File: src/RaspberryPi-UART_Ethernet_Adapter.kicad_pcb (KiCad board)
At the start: 2 copper layers, 67 x 40 mm, 28 parts, among them J101 Conn_02x06_Odd_Even, J102 Conn_01x06, J104 Conn_01x06, J105 Conn_02x05_Odd_Even, J106 USB4125-GF-A, J107 USB_B_Micro, J108 Barrel_Jack, U101 TLV1117-33

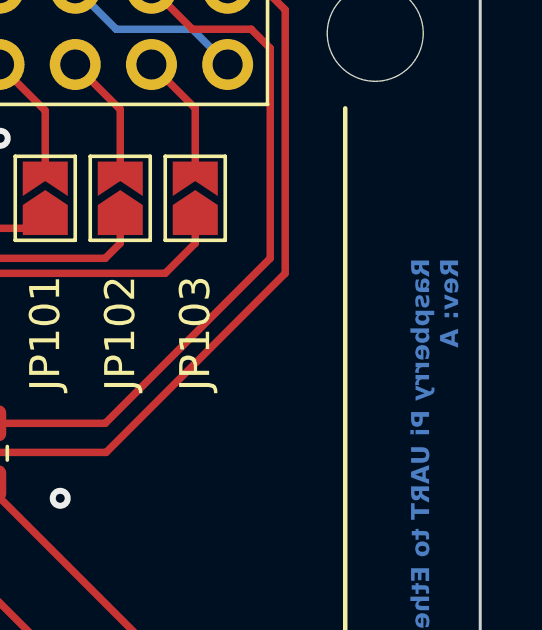
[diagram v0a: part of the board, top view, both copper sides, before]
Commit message: Mod: Footprint J106, added front paste layer, closes #1. Moved logo G1 in the middle of the plane, closes #4.
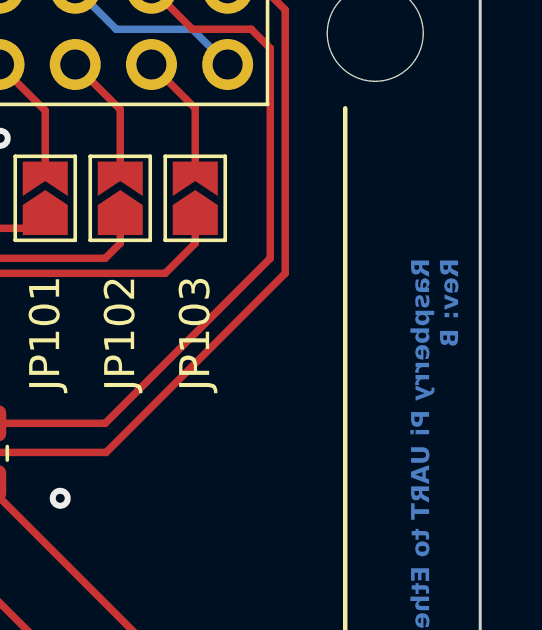
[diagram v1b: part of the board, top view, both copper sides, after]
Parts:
- moved G*** 1.25 mm to (176.8, 90.0)
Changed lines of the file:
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@@
 	(title_block
 		(title "Raspberry Pi UART to Ethernet Adapter")
-		(date "2024-03-03")
-		(rev "A")
+		(date "2024-03-15")
+		(rev "B")
 		(company "ElektroNik Zoller")
 		(comment 1 "Nikolai Zoller")
@@
 			(drillshape 0)
 			(scaleselection 1)
-			(outputdirectory "../gerbers")
+			(outputdirectory "../gerbers_${TITLE}_${REVISION}")
 		)
 	)
@@
 			)
 		)
-		(property "Footprint" ""
+		(property "Footprint" "MountingHole:MountingHole_2.7mm_M2.5_DIN965"
 			(at 0 0 0)
 			(unlocked yes)
@@
 			)
 		)
-		(property "Footprint" ""
+		(property "Footprint" "Resistor_SMD:R_0805_2012Metric_Pad1.20x1.40mm_HandSolder"
 			(at 0 0 -90)
 			(unlocked yes)
@@
 		)
 		(property "Manufacturer Part No." "RC0805FR-075K1L"
-			(at 0 0 0)
+			(at 0 0 180)
 			(layer "F.Fab")
 			(hide yes)
@@
 		)
 		(property "Vendor" "Digikey"
-			(at 0 0 0)
+			(at 0 0 180)
 			(layer "F.Fab")
 			(hide yes)
@@
 		)
 		(property "Vendor Part No." "311-5.10KCRCT-ND"
-			(at 0 0 0)
+			(at 0 0 180)
 			(layer "F.Fab")
 			(hide yes)
@@
 			)
 		)
-		(property "Footprint" ""
+		(property "Footprint" "Resistor_SMD:R_0805_2012Metric_Pad1.20x1.40mm_HandSolder"
 			(at 0 0 90)
 			(unlocked yes)
@@
 			)
 		)
-		(property "Footprint" ""
+		(property "Footprint" "LED_SMD:LED_0805_2012Metric_Pad1.15x1.40mm_HandSolder"
 			(at 0 0 -90)
 			(unlocked yes)
@@
 			)
 		)
-		(property "Footprint" ""
+		(property "Footprint" "Resistor_SMD:R_0805_2012Metric_Pad1.20x1.40mm_HandSolder"
 			(at 0 0 90)
 			(unlocked yes)
@@
 			)
 		)
-		(property "Footprint" ""
+		(property "Footprint" "MountingHole:MountingHole_2.7mm_M2.5_DIN965"
 			(at 0 0 0)
 			(unlocked yes)
@@
 			)
 		)
-		(property "Footprint" ""
+		(property "Footprint" "Connector_PinHeader_2.54mm:PinHeader_2x05_P2.54mm_Vertical"
 			(at 0 0 90)
 			(unlocked yes)
@@
 			)
 		)
-		(property "Manufacturer Part No." "RS2-10-G"
+		(property "Manufacturer Part No." "PH2-10-UA"
 			(at 0 0 0)
 			(layer "F.Fab")
@@
 			)
 		)
-		(property "Vendor Part No." "2057-RS2-10-G-ND"
+		(property "Vendor Part No." "2057-PH2-10-UA-ND"
 			(at 0 0 0)
 			(layer "F.Fab")
@@
 			)
 		)
-		(property "Footprint" ""
+		(property "Footprint" "MountingHole:MountingHole_3.2mm_M3_DIN965"
 			(at 0 0 0)
 			(unlocked yes)
@@
 			)
 		)
-		(property "Footprint" ""
+		(property "Footprint" "Capacitor_SMD:C_0805_2012Metric_Pad1.18x1.45mm_HandSolder"
 			(at 0 0 -90)
 			(unlocked yes)
@@
 			)
 		)
-		(property "Manufacturer Part No." "TLJP107M006R5400"
+		(property "Manufacturer Part No." "CL21A107MQYNNWE"
 			(at 0 0 0)
 			(layer "F.Fab")
@@
 			)
 		)
-		(property "Vendor Part No." "478-5260-1-ND"
+		(property "Vendor Part No." "1276-CL21A107MQYNNWECT-ND"
 			(at 0 0 0)
 			(layer "F.Fab")
@@
 			)
 		)
-		(property "Footprint" ""
+		(property "Footprint" "Capacitor_SMD:C_0805_2012Metric_Pad1.18x1.45mm_HandSolder"
 			(at 0 0 90)
 			(unlocked yes)
@@
 			)
 		)
-		(property "Footprint" ""
+		(property "Footprint" "Connector_USB:USB_Micro-B_Amphenol_10118194_Horizontal"
 			(at 0 0 0)
 			(unlocked yes)
@@
 			)
 		)
-		(property "Footprint" ""
+		(property "Footprint" "MountingHole:MountingHole_2.7mm_M2.5_DIN965"
 			(at 0 0 0)
 			(unlocked yes)
@@
 			)
 		)
-		(property "Footprint" ""
+		(property "Footprint" "Connector_User:CUI_PJ-037A_Board-Edge"
 			(at 0 0 180)
 			(unlocked yes)
@@
 			)
 		)
-		(property "Footprint" ""
+		(property "Footprint" "Jumper:SolderJumper-2_P1.3mm_Open_TrianglePad1.0x1.5mm"
 			(at 0 0 90)
 			(unlocked yes)
@@
 			)
 		)
-		(property "Footprint" ""
+		(property "Footprint" "Connector_PinSocket_2.54mm:PinSocket_1x06_P2.54mm_Vertical"
 			(at 0 0 90)
 			(unlocked yes)
@@
 			)
 		)
-		(property "Footprint" ""
+		(property "Footprint" "Connector_PinSocket_2.54mm:PinSocket_2x06_P2.54mm_Vertical"
 			(at 0 0 0)
 			(unlocked yes)
@@
 			)
 		)
-		(property "Footprint" ""
+		(property "Footprint" "MountingHole:MountingHole_3.2mm_M3_DIN965"
 			(at 0 0 0)
 			(unlocked yes)
@@
 			)
 		)
-		(property "Footprint" ""
+		(property "Footprint" "Resistor_SMD:R_0805_2012Metric_Pad1.20x1.40mm_HandSolder"
 			(at 0 0 -90)
 			(unlocked yes)
@@
 			)
 		)
-		(property "Footprint" ""
+		(property "Footprint" "Jumper:SolderJumper-2_P1.3mm_Open_TrianglePad1.0x1.5mm"
 			(at 0 0 90)
 			(unlocked yes)
@@
 			)
 		)
-		(property "Footprint" ""
+		(property "Footprint" "Jumper:SolderJumper-2_P1.3mm_Open_TrianglePad1.0x1.5mm"
 			(at 0 0 90)
 			(unlocked yes)
@@
 			)
 		)
-		(property "Footprint" ""
+		(property "Footprint" "Package_TO_SOT_SMD:SOT-223-3_TabPin2"
 			(at 0 0 90)
 			(unlocked yes)
@@
 			)
 		)
-		(property "Datasheet" ""
+		(property "Datasheet" "http://www.ti.com/lit/ds/symlink/tlv1117.pdf"
 			(at 0 0 90)
 			(unlocked yes)
@@
 			)
 		)
-		(property "Footprint" ""
+		(property "Footprint" "LED_SMD:LED_0805_2012Metric_Pad1.15x1.40mm_HandSolder"
 			(at 0 0 -90)
 			(unlocked yes)
@@
 			)
 		)
-		(property "Footprint" ""
+		(property "Footprint" "MountingHole:MountingHole_3.2mm_M3_DIN965"
 			(at 0 0 0)
 			(unlocked yes)
@@
 			)
 		)
-		(property "Footprint" ""
+		(property "Footprint" "MountingHole:MountingHole_3.2mm_M3_DIN965"
 			(at 0 0 0)
 			(unlocked yes)
@@
 			)
 		)
-		(property "Footprint" ""
+		(property "Footprint" "Connector_User:GCT_USB4125-GF-A"
 			(at 0 0 0)
 			(unlocked yes)
@@
 			(size 1 1.6)
 			(drill oval 0.6 1.2)
-			(layers "*.Cu")
+			(layers "*.Cu" "F.Paste")
 			(remove_unused_layers no)
 			(net 2 "GND")
@@
 			(size 1 1.6)
 			(drill oval 0.6 1.2)
-			(layers "*.Cu")
+			(layers "*.Cu" "F.Paste")
 			(remove_unused_layers no)
 			(net 2 "GND")
@@
 			(size 1 1.6)
 			(drill oval 0.6 1.2)
-			(layers "*.Cu")
+			(layers "*.Cu" "F.Paste")
 			(remove_unused_layers no)
 			(net 2 "GND")
@@
 			(size 1 1.6)
 			(drill oval 0.6 1.2)
-			(layers "*.Cu")
+			(layers "*.Cu" "F.Paste")
 			(remove_unused_layers no)
 			(net 2 "GND")
@@
 			)
 		)
-		(property "Footprint" ""
+		(property "Footprint" "Connector_PinSocket_2.54mm:PinSocket_1x06_P2.54mm_Vertical"
 			(at 0 0 90)
 			(unlocked yes)
@@
 			)
 		)
-		(property "Footprint" ""
+		(property "Footprint" "MountingHole:MountingHole_2.7mm_M2.5_DIN965"
 			(at 0 0 0)
 			(unlocked yes)
@@
 	(footprint "Drawings_User:elektronik-emblem_10x11.6_solder"
 		(layer "B.Cu")
-		(at 175.5 90 180)
+		(at 176.75 90 180)
 		(property "Reference" "G***"
 			(at 0 0 0)
